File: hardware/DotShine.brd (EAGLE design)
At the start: 30 x 65 mm, 58 parts, among them CN1 1X4-BIG, IC1 CAT24M010TS, IC3 SI1145, J3 USB-MICROB, U1 ATMEGA328P-MU-QFN32, U2 TMP102, U3 ATSHA204-TSU, X2 MC-RTC-RV-4162-C7-I2C, X3 S4B-ZR

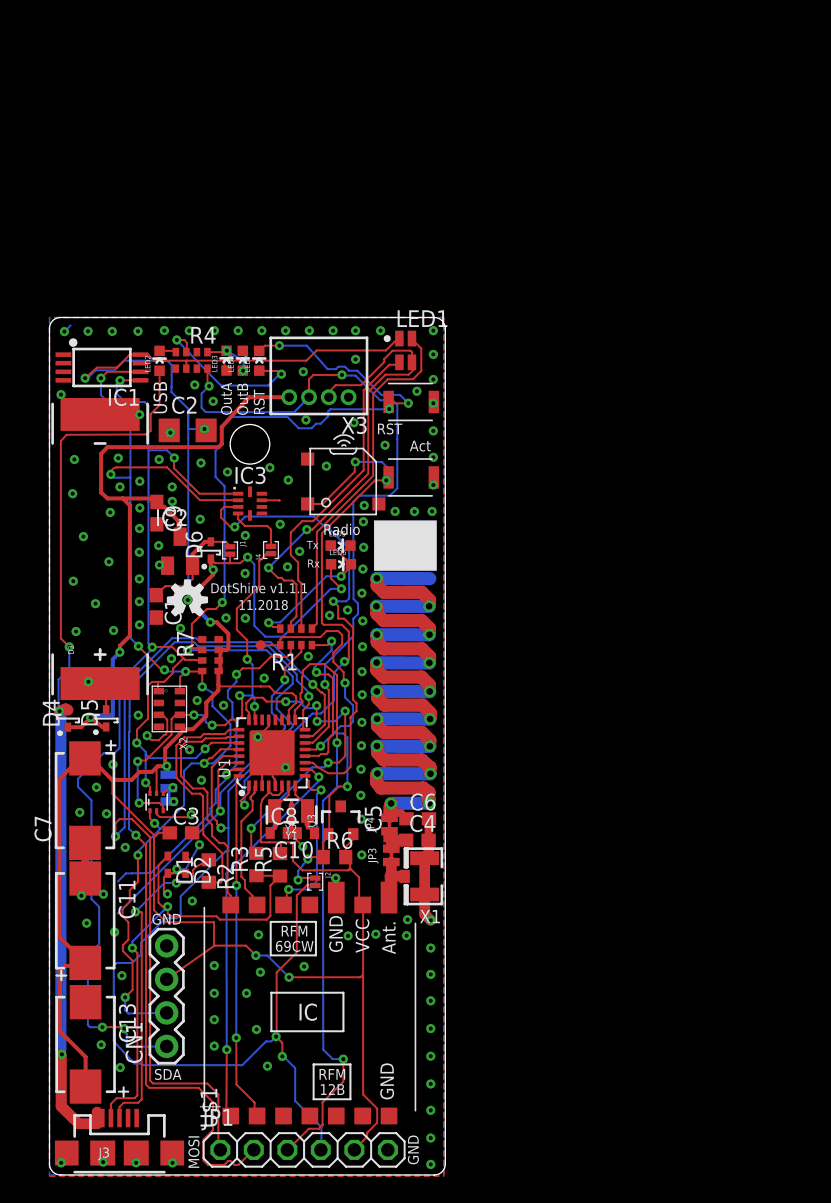
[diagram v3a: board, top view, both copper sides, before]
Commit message: Initial version with BLE using JDY-16
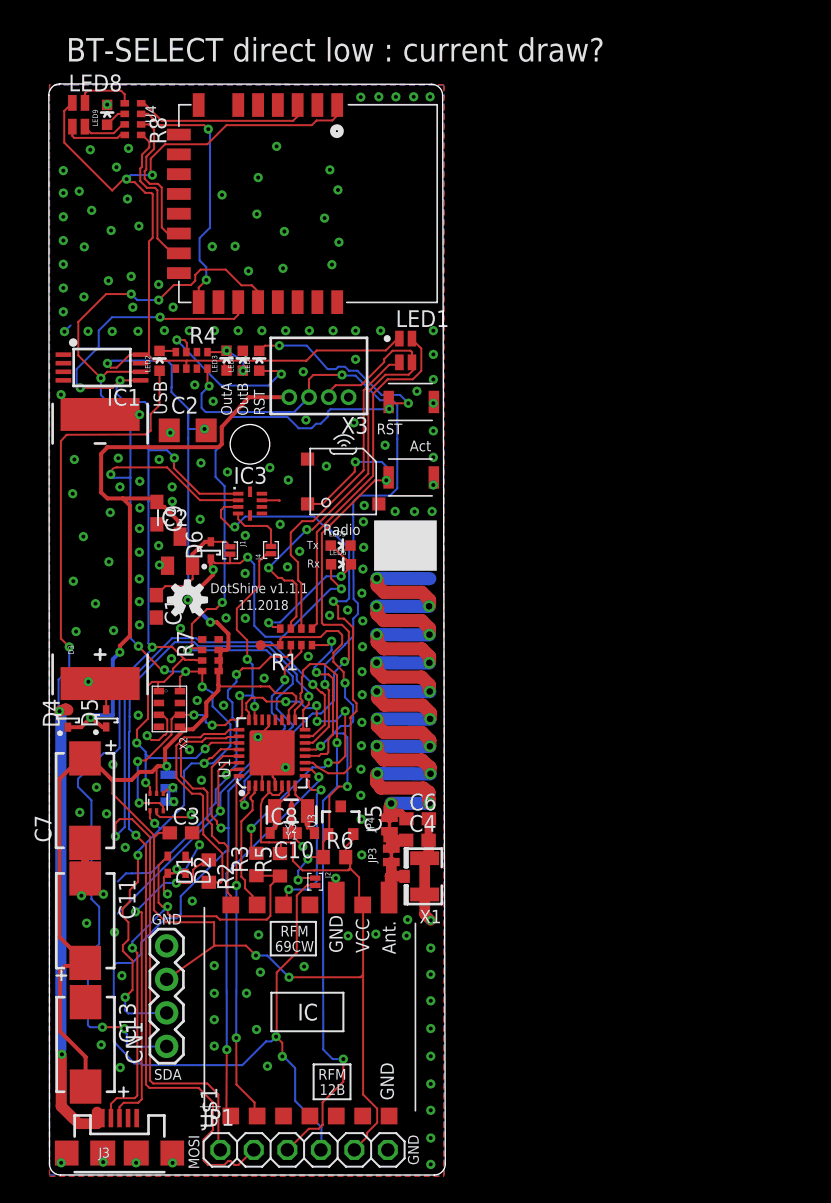
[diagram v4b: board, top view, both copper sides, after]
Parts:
- added LED8: GM1WA55311A, led:GM1WA55311A
- added LED9: (no value), SparkFun:LED-0603
- added R8: (no value), SparkFun:0603-ARV
- added U4: JDY-16, altro:JDY-16
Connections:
- new net ALED: R8.3, U4.17
- new net BT_BLUE: LED8.2, R8.8
- new net BT_GREEN: LED8.3, R8.7
- new net BT_RED: LED8.1, R8.5
- new net N$34: LED9.A, R8.6
- new net PWM1: U4.2
- new net PWM2: R8.4, U4.3
- new net PWM3: R8.2, U4.14
- new net PWM4: R8.1, U4.15
- net +3V3: now also LED8.4, U4.1
- net GND: now also LED9.C, U4.21, U4.24
- net SCL: now also U4.20
- net SDA: now also U4.19
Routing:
- net +3V3: track 223.6 -> 263.9 mm, vias 10 -> 12
- net SCL: track 85.9 -> 108.3 mm, vias 10 -> 12
- net SDA: track 97.9 -> 118.5 mm, vias 8 -> 10
- net ALED: track 0.00 -> 19.5 mm, vias 0 -> 2
- net PWM2: track 0.00 -> 13.4 mm
- net PWM4: track 0.00 -> 11.3 mm
- net PWM3: track 0.00 -> 11.2 mm
- net BT_BLUE: track 0.00 -> 4.82 mm
- net BT_RED: track 0.00 -> 4.62 mm
- net BT_GREEN: track 0.00 -> 3.52 mm
- net N$34: track 0.00 -> 1.67 mm
- net GND: vias 148 -> 190
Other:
- board size 30 x 65 mm -> 30.1 x 82.7 mm
- board text added: "BT-SELECT direct low : current draw?"

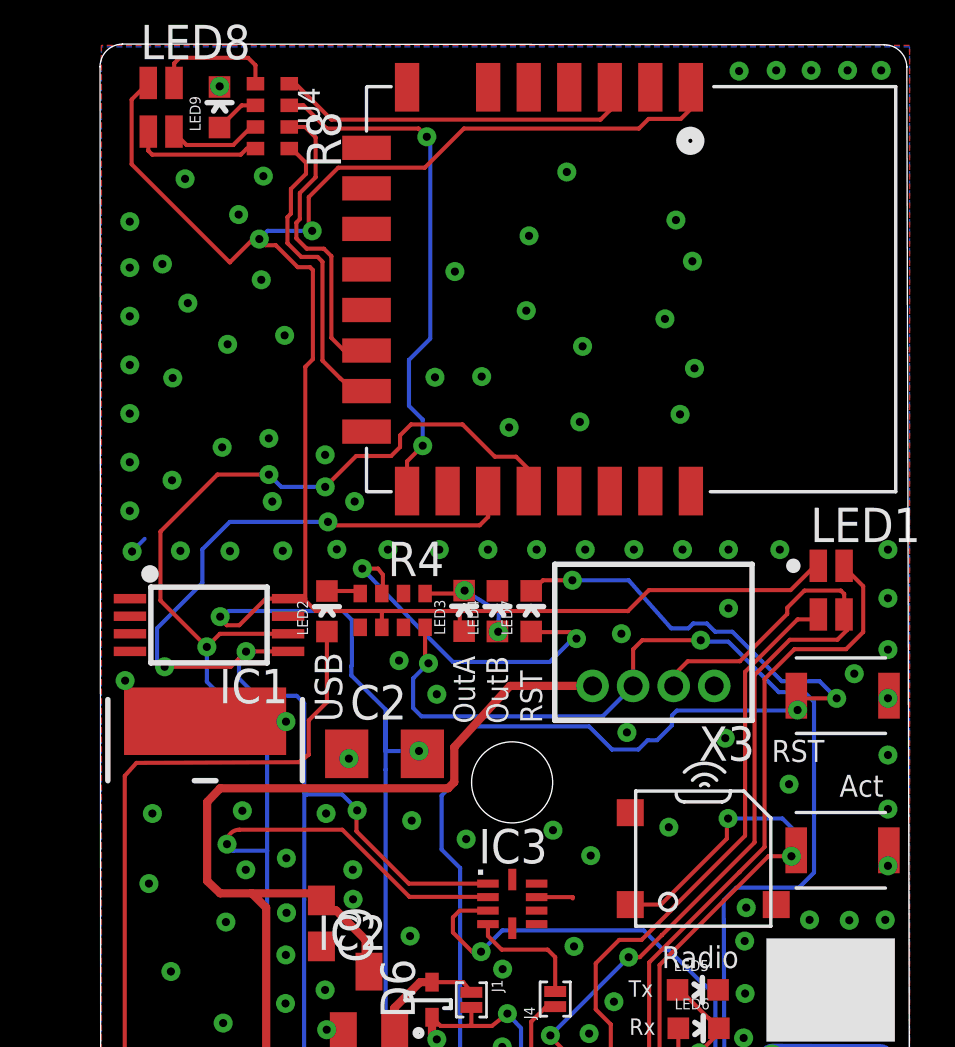
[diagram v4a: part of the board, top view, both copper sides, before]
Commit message: Initial bluetooth integration
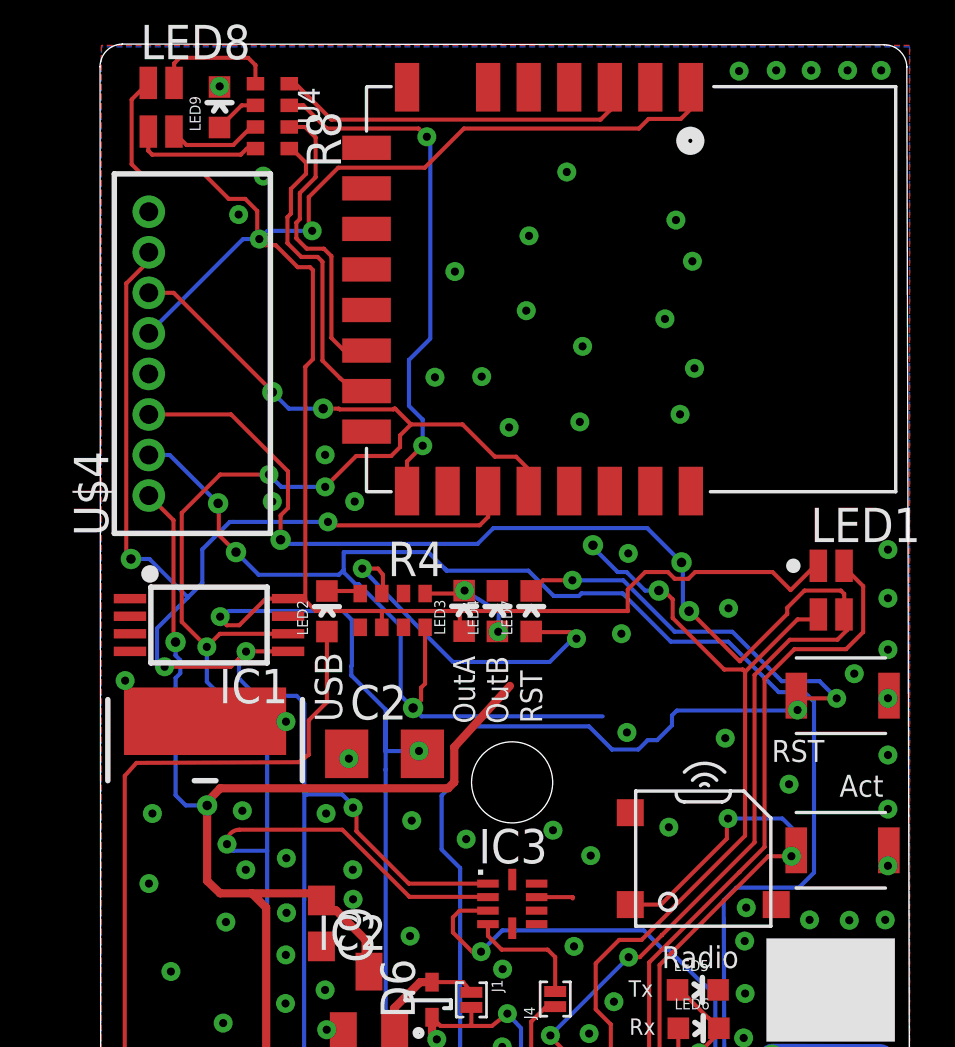
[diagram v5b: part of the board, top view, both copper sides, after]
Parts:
- removed X3: S4B-ZR, con-jst:S4B-ZR
- added U$4: JST-8, mihai_connectors_jst:S4B-ZR
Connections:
- removed net N$4: LED1.2, R1.6
- new net RXD_IN: LED1.2, R1.6, U$4.8
- net +3V3: now also U$4.5
- net +5V: now also U$4.1; no longer X3.4
- net GND: now also U$4.4; no longer X3.1
- net OUTAB: now also U$4.2; no longer X3.3
- net SCL: now also U$4.6
- net SDA: now also U$4.7
- net TXD_OUT: now also U$4.3; no longer X3.2
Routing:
- net RXD_IN: track 0.00 -> 33.2 mm, vias 0 -> 2
- net TXD_OUT: track 36.6 -> 62.7 mm, vias 2 -> 5
- net OUTAB: track 52.0 -> 77.6 mm, vias 3 -> 4
- net N$4: track 25.1 -> 0.00 mm
- net SDA: track 118.5 -> 133.0 mm, vias 10 -> 11
- net SCL: track 108.3 -> 119.4 mm, vias 12 -> 14
- net +5V: track 50.3 -> 60.2 mm, vias 2 -> 4
- net +3V3: track 263.9 -> 270.6 mm
- net GND: track 39.2 -> 38.6 mm, vias 190 -> 158

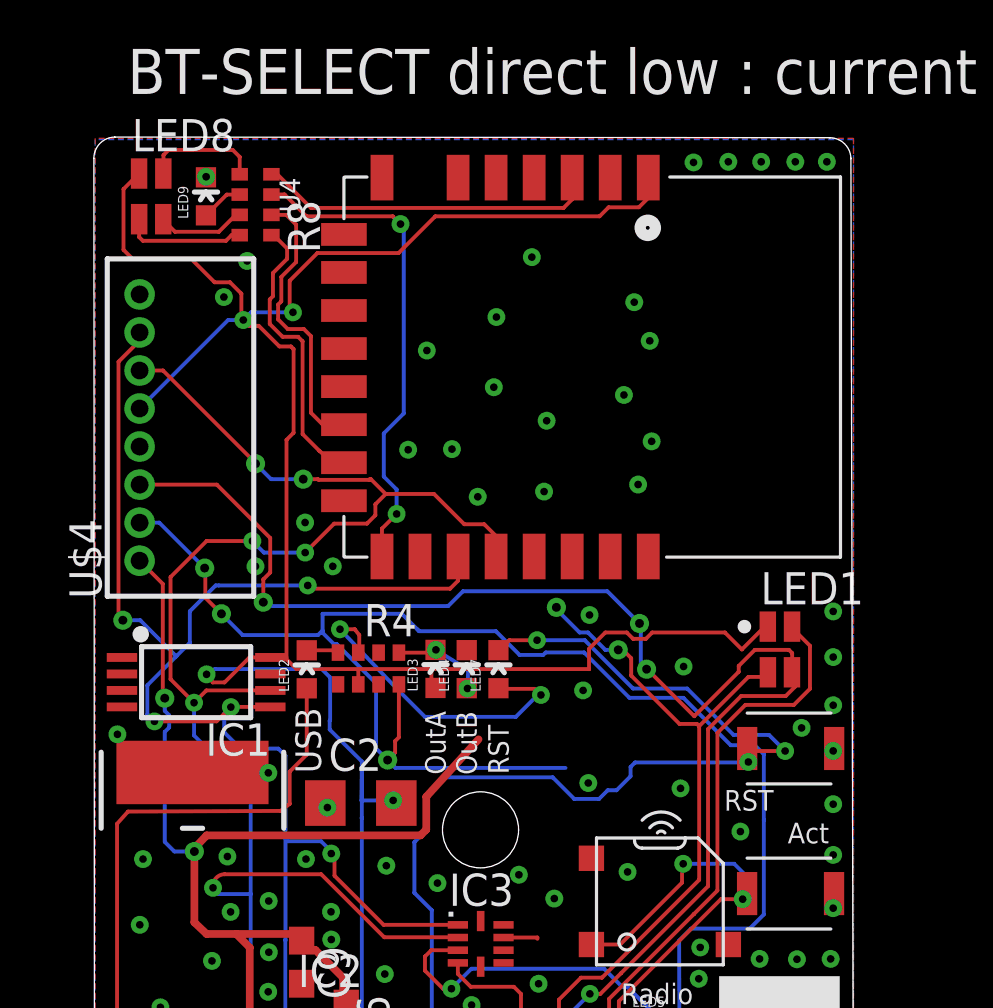
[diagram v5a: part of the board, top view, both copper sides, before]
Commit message: Add and flip JST8, add BLE logo
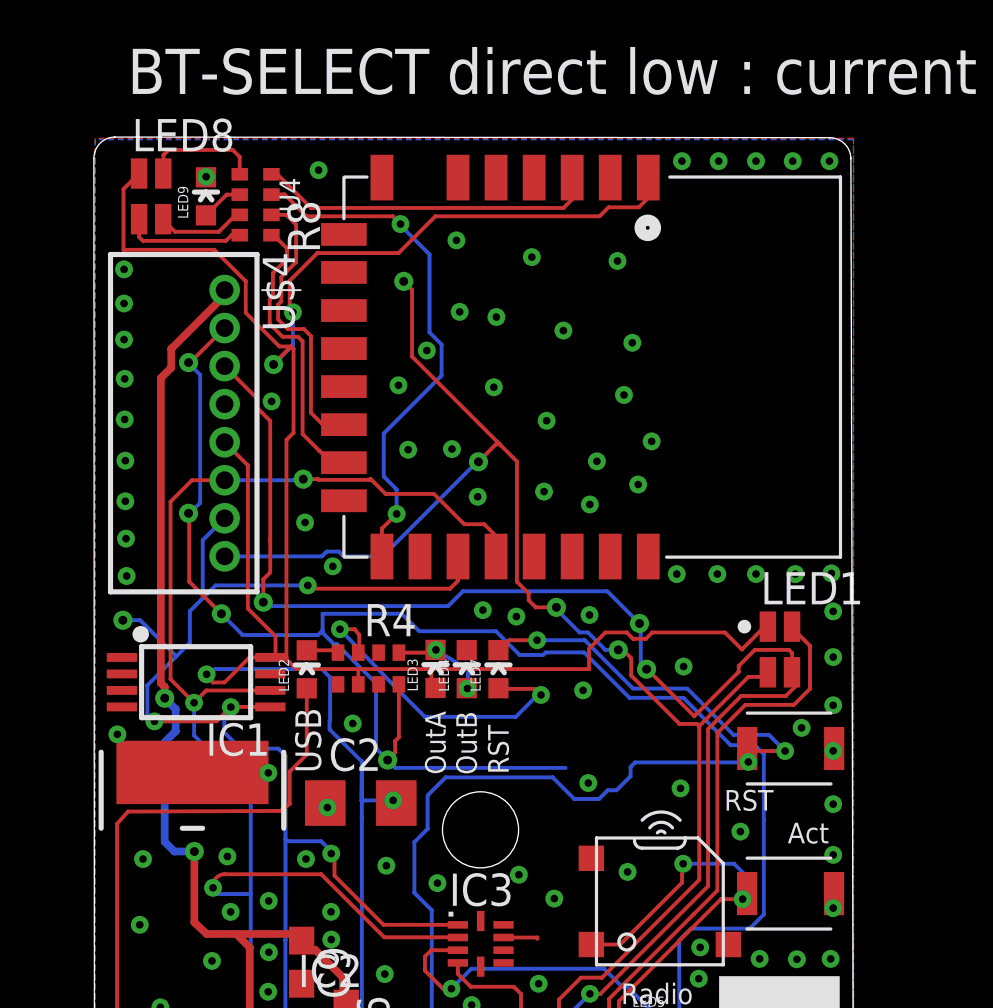
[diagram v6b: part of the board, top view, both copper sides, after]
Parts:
- moved U$4 7.02 mm to (5.11, 74.4), turned to 270 degrees
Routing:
- net RXD_IN: track 33.2 -> 61.9 mm, vias 2 -> 4
- net SCL: track 119.4 -> 109.2 mm, vias 14 -> 11
- net SDA: track 133.0 -> 124.9 mm
- net OUTAB: track 77.6 -> 85.0 mm, vias 4 -> 5
- net +3V3: track 270.6 -> 275.8 mm
- net +5V: track 60.2 -> 57.8 mm
- net TXD_OUT: track 62.7 -> 64.2 mm
- net ALED: track 19.5 -> 20.9 mm
- net GND: vias 158 -> 180
